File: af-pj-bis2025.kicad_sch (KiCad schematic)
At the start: 81 parts, among them J1 CN7, J2 CN10, J3 Conn_01x06, J4 Conn_Coaxial, J5 Barrel_Jack_MountingPin, J7 Conn_Coaxial, J8 Conn_01x10, U1 MIC5237-5.0YU, U2 ALD114904APAL, U3 OPA2380AIDGKR, U4 THS4552IPWR, U5 REF5050IDR, U6 LT1991ACMS-TRPBF, U7 UA78L06ACPK, U8 ADS1220IPW

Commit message: DRC,LVSクリアとテストピン、デバック用ピン追加
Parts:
- removed J3: Conn_01x06, Connector_PinSocket_2.54mm:PinSocket_1x06_P2.54mm_Vertical, symbol Connector_Generic:Conn_01x06
- added J10, J11, J8, J9: Conn_01x02, Connector_PinHeader_2.54mm:PinHeader_1x02_P2.54mm_Vertical, symbol Connector_Generic:Conn_01x02
- added J7: Conn_01x06, Connector_PinHeader_2.54mm:PinHeader_1x06_P2.54mm_Vertical, symbol Connector_Generic:Conn_01x06
- added TP1, TP10, TP11, TP12, TP13, TP14, TP15, TP16, TP2, TP3, TP4, TP7, TP8, TP9: TestPoint, Connector_Pin:Pin_D1.0mm_L10.0mm, symbol Connector:TestPoint
- renumbered C8 to C10, C9 to C11, C10 to C12, C11 to C13, C12 to C14, C13 to C15, C14 to C16, C15 to C17, C16 to C18, C25 to C19, C26 to C20, C28 to C21, C27 to C22, C17 to C23, C29 to C24, C30 to C25, C18 to C26, C19 to C27, C20 to C28, C21 to C29, C22 to C30, C23 to C31, C31 to C32, C32 to C33, C33 to C34, C24 to C35, C35 to C6, C6 to C7, C34 to C8, C7 to C9, J5 to J1, J1 to J2, J7 to J3, J2 to J5, J8 to J6, Re1 to R1, Re8 to R10, Re9 to R11, Re10 to R12, Re11 to R13, Re12 to R14, Re13 to R15, Re14 to R16, Re15 to R17, Re25 to R18, Re26 to R19, Re2 to R2, Re27 to R20, Re16 to R21, Re17 to R22, Re28 to R23, Re29 to R24, Re18 to R25, Re19 to R26, Re20 to R27, Re21 to R28, Re22 to R29, Re3 to R3, Re23 to R30, Re24 to R31, Re4 to R4, R1 to R5, R2 to R6, Re5 to R7, Re6 to R8, Re7 to R9
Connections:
- net LCD_EXCOMIN is gone; now on net LCD_EXTCOMIN: J6.7 (Pin_7)
- net ADC_CS: now also J2.28 (Pin_28), TP7.1; no longer J5.21 (Pin_21)
- net ADC_DRDY: now also J2.30 (Pin_30), TP11.1; no longer J5.26 (Pin_26)
- net ADC_MISO: now also TP10.1
- net ADC_MOSI: now also TP9.1
- net ADC_SCLK: now also J5.30 (Pin_30), TP8.1; no longer J5.25 (Pin_25)
- net AIN1N: now also TP3.1
- net AIN1P: now also TP4.1
- net AIN2_adcN: now also J7.3 (Pin_3)
- net AIN2_adcP: now also J7.4 (Pin_4)
- net AIN2_inN: now also J7.2 (Pin_2)
- net AIN2_inP: now also J7.5 (Pin_5)
- net AIN2_mcuN: now also J2.37 (Pin_37), J7.1 (Pin_1)
- net AIN2_mcuP: now also J2.38 (Pin_38), J7.6 (Pin_6)
- net AVDD_5V: now also TP12.1
- net AVDD_6.2V: now also TP14.1
- net AVSS: now also J1.3 (MountPin), J8.2 (Pin_2), J9.2 (Pin_2); no longer J1.MP (MountPin)
- net DC_9V: now also TP13.1
- net GATE1: now also J8.1 (Pin_1)
- net GATE2: now also J9.1 (Pin_1)
- net GND: now also J5.9 (Pin_9)
- net LCD_DISP: now also J5.36 (Pin_36); no longer J2.1 (Pin_1)
- net OUT1: now also TP2.1
- net OUT2: now also TP1.1
- net VDDA: now also J5.7 (Pin_7)
- net VREF_0.5V: now also TP16.1
- net VREF_5V: now also TP15.1
- net at C4.2, R1.2, U3.2 (INA-): now also J10.2 (Pin_2); no longer U2.3 (DN1)
- net at C5.2, R2.2, U3.6 (INB-): now also J11.2 (Pin_2); no longer U2.6 (DN2)
- new net: J10.1 (Pin_1), U2.3 (DN1)
- new net: J11.1 (Pin_1), U2.6 (DN2)
- no-connect marks 7 -> 59
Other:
- moved on the sheet: C19, C20, C21, C22, C24, C25, C32, C33, C34, C6, C8, J2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

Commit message: 回路が完成した
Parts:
- added TP5: TestPoint, Connector_Pin:Pin_D1.0mm_L10.0mm, symbol Connector:TestPoint
- renumbered TP8 to TP10, TP9 to TP8, TP10 to TP9
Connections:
- net GND: now also C34.2, U8.4 (DGND)
- net GNDA: now also C1.2, C10.1, C11.1, C12.1, C14.1, C18.1, C19.2, C2.2, C20.2, C21.2, C22.2, C24.2, C25.2, C27.1, C3.2, C31.1, C32.2, C33.2, C7.1, C9.1, J1.2, J1.3 (MountPin), J3.2 (Ext), J4.2 (Ext), J8.2 (Pin_2), J9.2 (Pin_2), R14.1, R29.1, U1.2 (GND), U1.4, U2.4 (S12), U2.5 (V-), U3.4 (V-), U4.12 (VS-), U4.16 (VS-), U5.4 (GND), U6.3 (P9), U6.4 (VEE), U7.2 (COMMON), U8.3 (CLK), U8.5 (AVSS), U8.8 (REFN0), TP5.1
- removed net AVSS: C1.2, C10.1, C11.1, C12.1, C14.1, C18.1, C19.2, C2.2, C20.2, C21.2, C22.2, C24.2, C25.2, C27.1, C3.2, C31.1, C32.2, C33.2, C34.2, C7.1, C9.1, J1.2, J1.3 (MountPin), J3.2 (Ext), J4.2 (Ext), J8.2 (Pin_2), J9.2 (Pin_2), R14.1, R29.1, U1.2 (GND), U1.4, U2.4 (S12), U2.5 (V-), U3.4 (V-), U4.12 (VS-), U4.16 (VS-), U5.4 (GND), U6.3 (P9), U6.4 (VEE), U7.2 (COMMON), U8.3 (CLK), U8.4 (DGND), U8.5 (AVSS), U8.8 (REFN0)
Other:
- moved on the sheet: C1, C13, C14, C15, C16, C17, C18, C19, C2, C20, C21, C22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

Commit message: initial commit
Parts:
- removed U1: MIC5237-5.0YU, pj-bis2025:MIC5237-TO-263-3_MCL-M, symbol pj-bis2025:MIC5237-5.0YU
- added D1: LED, LED_SMD:LED_0805_2012Metric_Pad1.15x1.40mm_HandSolder, symbol Device:LED
- added J12: FH28-10S-0.5SH_05_, pj-bis2025:HIROSE_FH28-10S-0.5SH_05_, symbol pj-bis2025:FH28-10S-0.5SH_05_
- added R32, R33, R34, R35: 47, Resistor_SMD:R_0805_2012Metric_Pad1.20x1.40mm_HandSolder, symbol Device:R
- added R36: 698, Resistor_SMD:R_0805_2012Metric_Pad1.20x1.40mm_HandSolder, symbol Device:R
- added R37: 10k, Resistor_SMD:R_0805_2012Metric_Pad1.20x1.40mm_HandSolder, symbol Device:R
- added SW1, SW2: PTS 647 SN50 SMTR2 LFS, pj-bis2025:PTS_647_SN50_SMTR2_LFS_PTS 647 SN50 SMTR2 LFS-M, symbol pj-bis2025:PTS_647_SN50_SMTR2_LFS
- added U1: MIC5237-5.0YT, pj-bis2025:MIC5237_5_0YT, symbol pj-bis2025:MIC5237-5.0YT
- C1: footprint pj-bis2025:LDO_5V_out_TAJR105K016RNJAC_TAJR_AVX -> Capacitor_SMD:C_0805_2012Metric_Pad1.18x1.45mm_HandSolder
- C11, C9: value 3.18n -> 47n
- C12, C7: value 0.1u -> 47n
- C20, C6, C8: value 0.1u -> 0.1u_pass
- C4, C5: value 3.18n -> 4.7n
- R3, R4: value 50k -> 2.4k
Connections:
- net +3V3: now also J12.3, J12.4, J12.5, SW2.3, SW2.4
- net AVDD_5V: now also U1.3 (OUT)
- net DC_9V: now also D1.2 (A), U1.1 (IN)
- net GND: now also J12.1, J12.2, R37.1, SW1.3, SW1.4
- net GNDA: now also R36.1, U1.2 (GND)
- net LCD_CS: now also R33.1; no longer J6.8 (Pin_8)
- net LCD_DISP: now also J12.6
- net LCD_EXTCOMIN: now also R32.1; no longer J6.7 (Pin_7)
- net LCD_MOSI: now also R34.1; no longer J6.9 (Pin_9)
- net LCD_SCLK: now also R35.1; no longer J6.10 (Pin_10)
- net ~{RST}: now also SW1.1, SW1.2
- net at J2.23 (Pin_23): now also R37.2, SW2.1, SW2.2
- new net: J12.7, J6.7 (Pin_7), R32.2
- new net: D1.1 (K), R36.2
- new net: J12.9, J6.9 (Pin_9), R34.2
- new net: J12.10, J6.10 (Pin_10), R35.2
- new net: J12.8, J6.8 (Pin_8), R33.2
- no-connect marks 59 -> 57
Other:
- moved on the sheet: C1, TP12

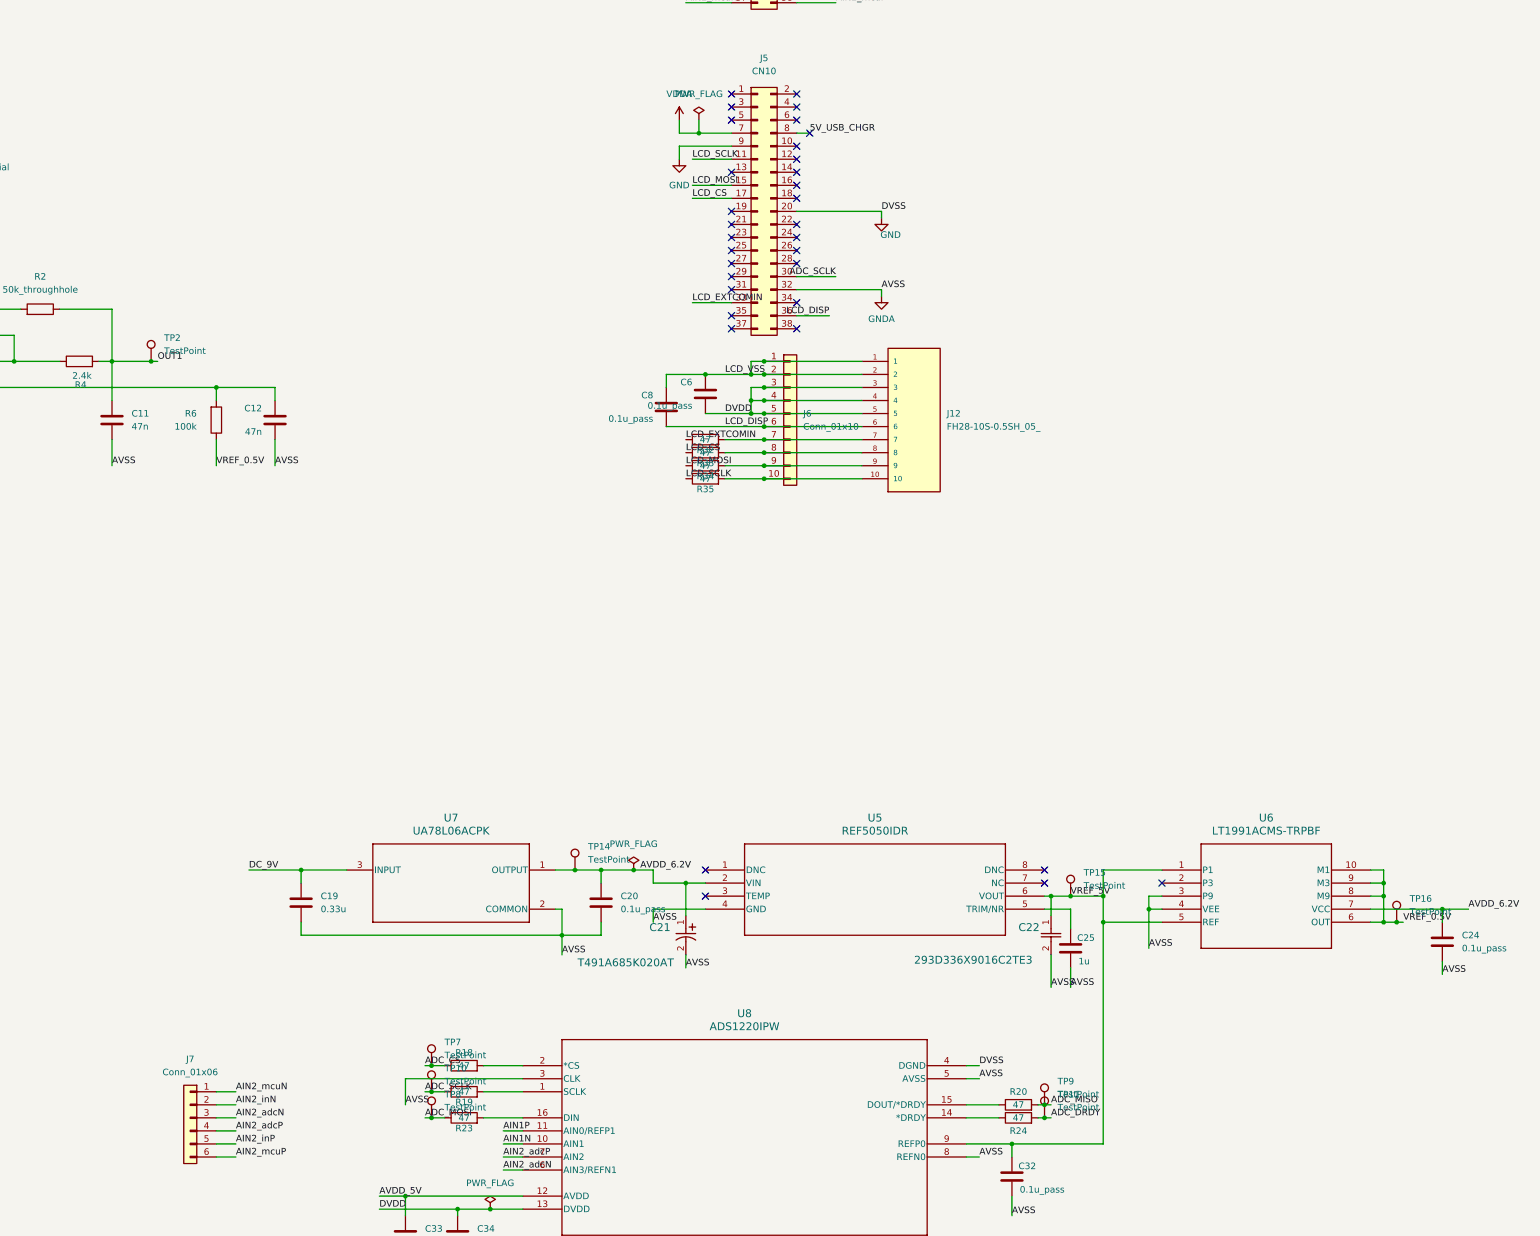
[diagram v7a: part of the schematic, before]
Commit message: change PCB layout
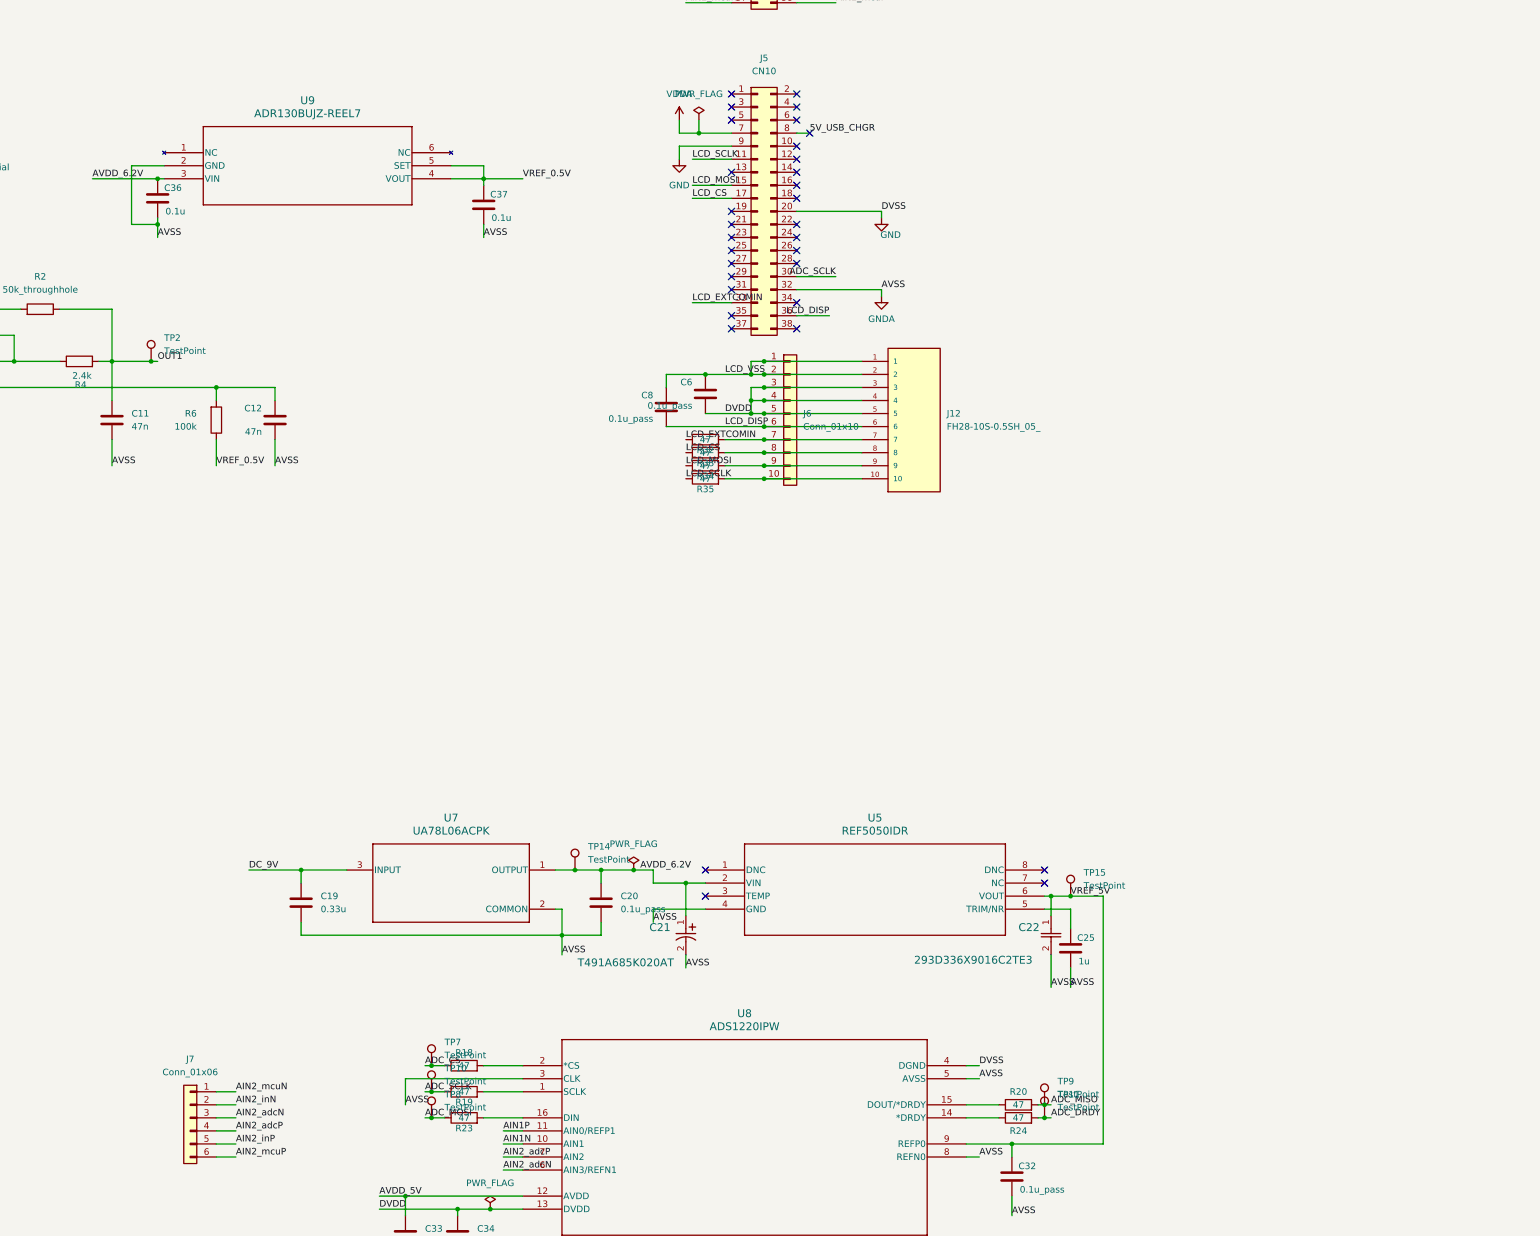
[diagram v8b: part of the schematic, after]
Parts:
- removed C24: 0.1u_pass, Capacitor_SMD:C_0805_2012Metric_Pad1.18x1.45mm_HandSolder, symbol Device:C
- removed TP16: TestPoint, Connector_Pin:Pin_D1.0mm_L10.0mm, symbol Connector:TestPoint
- removed U6: LT1991ACMS-TRPBF, pj-bis2025:LT1991-MSOP-10_MS_LIT-M, symbol pj-bis2025:LT1991ACMS-TRPBF
- added C36, C37: 0.1u, Capacitor_SMD:C_0805_2012Metric_Pad1.18x1.45mm_HandSolder, symbol Device:C
- added U9: ADR130BUJZ-REEL7, UJ_6_ADI, symbol pj-bis2025:ADR130BUJZ-REEL7
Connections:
- net AVDD_6.2V: now also C36.1, U9.3 (VIN)
- net GNDA: now also C36.2, C37.2, U9.2 (GND)
- net VREF_0.5V: now also C37.1, U9.4 (VOUT), U9.5 (SET)
- no-connect marks 57 -> 56
